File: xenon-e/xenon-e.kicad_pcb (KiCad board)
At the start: 2 copper layers, 133.7 x 105.5 mm, 86 parts, among them J1 MJ-4PP-9, P1 CONN_01X01, P2 CONN_01X01, P3 OLED, P4 LED, P5 ICSP, SW1 SW_PUSH, SW10 SW_PUSH, SW11 SW_PUSH, SW12 SW_PUSH, SW13 SW_PUSH, SW14 SW_PUSH, SW15 SW_PUSH, SW16 SW_PUSH, SW17 SW_PUSH, SW18 SW_PUSH, SW2 SW_PUSH, SW21 SW_PUSH, SW22 SW_PUSH, SW23 SW_PUSH, SW24 SW_PUSH, SW25 SW_PUSH, SW29 SW_PUSH, SW3 SW_PUSH, SW30 SW_PUSH, SW31 SW_PUSH, SW32 SW_PUSH, SW33 Reset, SW4 SW_PUSH, SW5 SW_PUSH, SW6 SW_PUSH, SW7 SW_PUSH, SW8 SW_PUSH, SW9 SW_PUSH, U1 ProMicro

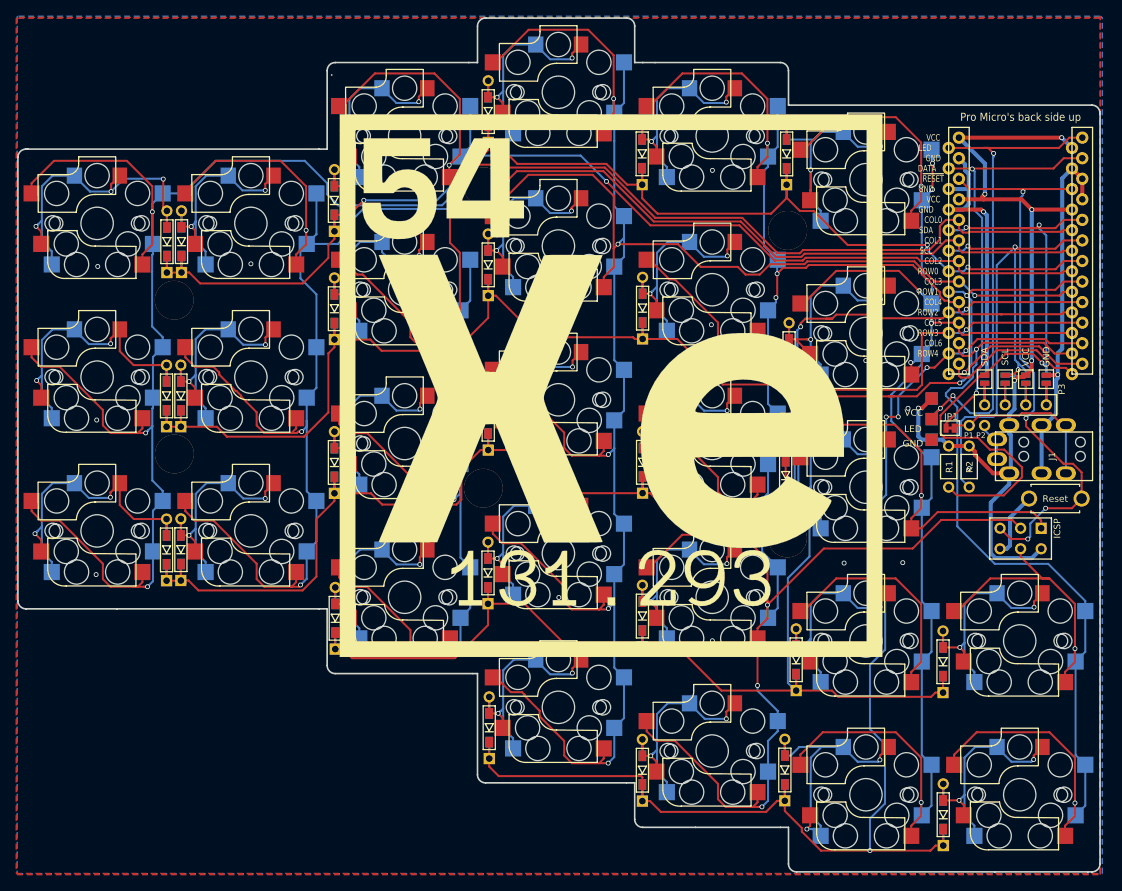
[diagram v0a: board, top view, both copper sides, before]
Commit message: Change mouting hole size
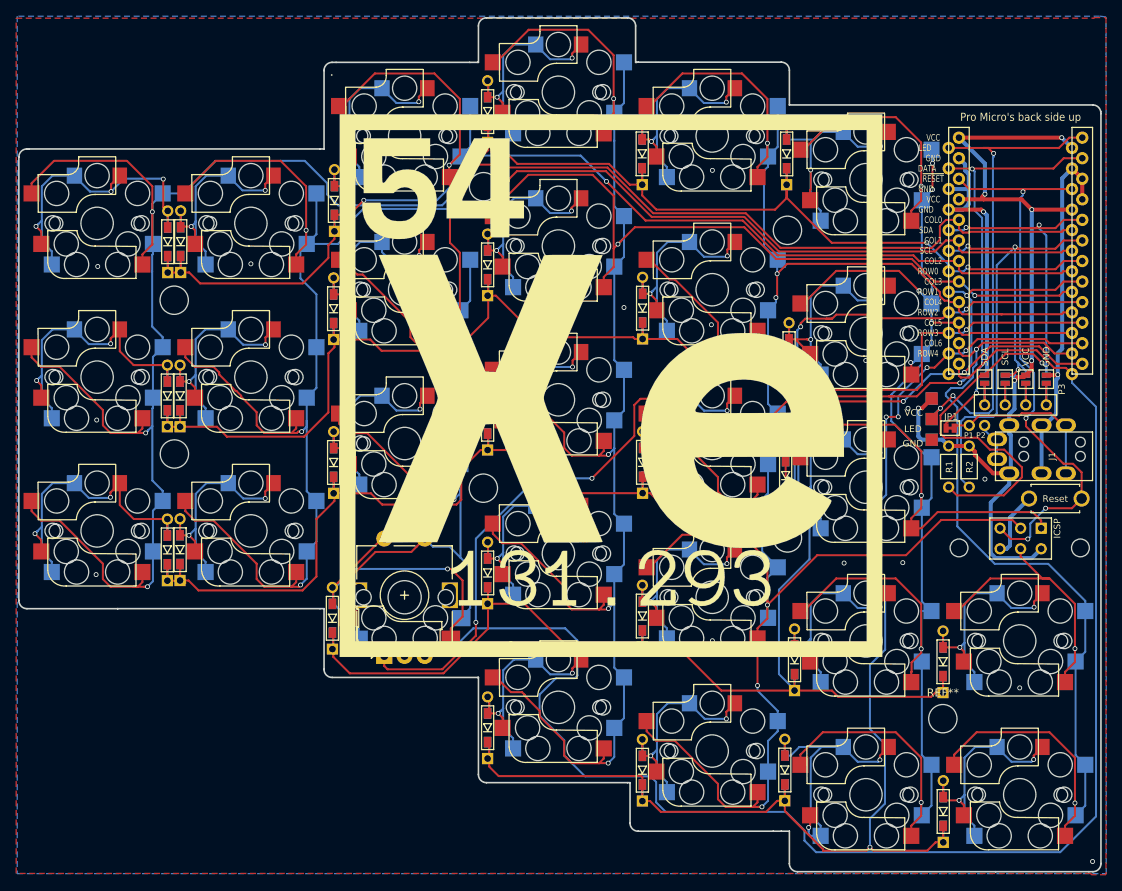
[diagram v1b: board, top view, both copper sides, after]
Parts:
- added REF**: MountingHole_2.2mm_M2, MountingHole:MountingHole_2.2mm_M2, F.Cu at (213.5, 98.5)
- added REF**: MountingHole_2.2mm_M2, MountingHole:MountingHole_2.2mm_M2, F.Cu at (198.5, 98.5)
- added REF**: MountingHole_3.5mm, MountingHole:MountingHole_3.5mm, F.Cu at (196.5, 119.6)
- added SW34: Rotary_Encoder_Switch, Rotary_Encoder:RotaryEncoder_Alps_EC11E-Switch_Vertical_H20mm, F.Cu at (127.5, 111.8)
- Ref** (x6): footprint kbd:M2_HOLE_v2 -> MountingHole:MountingHole_3.5mm
- SW21: footprint kbd:CherryMX_Choc_Hotswap -> foostan_kbd:CherryMX_Hotswap
- moved D32 0.40 mm to (196.6, 131.1)
- moved D21 0.35 mm to (121.1, 107.2)
- moved D24 0.20 mm to (178.2, 112.3)
- moved D29 0.20 mm to (140.2, 120.7)
- moved D13 0.10 mm to (100.7, 98.7)
- moved D15 0.10 mm to (121.2, 87.9)
- moved D7 0.10 mm to (100.7, 79.7)
- moved D9 0.10 mm to (121.2, 68.9)
- moved D1 0.10 mm to (100.7, 60.7)
- moved D14 0.10 mm to (102.2, 98.7)
- moved D2 0.10 mm to (102.3, 60.7)
- moved D8 0.10 mm to (102.2, 79.7)
- moved D16 0.07 mm to (140.2, 82.6)
- moved D4 0.07 mm to (140.2, 44.6)
- moved D10 0.07 mm to (140.2, 63.5)
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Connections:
- net /ex1 renamed ROTARY_A
- net /ex2 renamed ROTARY_B
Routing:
- net ROTARY_B: track 18.2 -> 188.4 mm
- net ROTARY_A: track 18.8 -> 117.4 mm, vias 1 -> 4
- net Net-(D21-Pad2): track 30.6 -> 44.3 mm, vias 2 -> 1
- net col2: track 263.5 -> 258.0 mm, vias 5 -> 4
- net row3: track 186.9 -> 190.4 mm
- net col4: track 296.6 -> 295.2 mm
- net col5: track 269.6 -> 270.3 mm, vias 8 -> 9
- net col1: track 236.0 -> 235.4 mm
- net col0: track 256.3 -> 255.7 mm
- net row0: track 160.9 -> 160.3 mm
- net GND: vias 17 -> 23
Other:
- outline, holes or cut-outs redrawn
- board text added: "Xenon v1.2.0 + rotary"
- board text removed: "Xenon Keyboard PCB v1.00"
